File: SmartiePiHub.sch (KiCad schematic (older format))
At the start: 91 parts

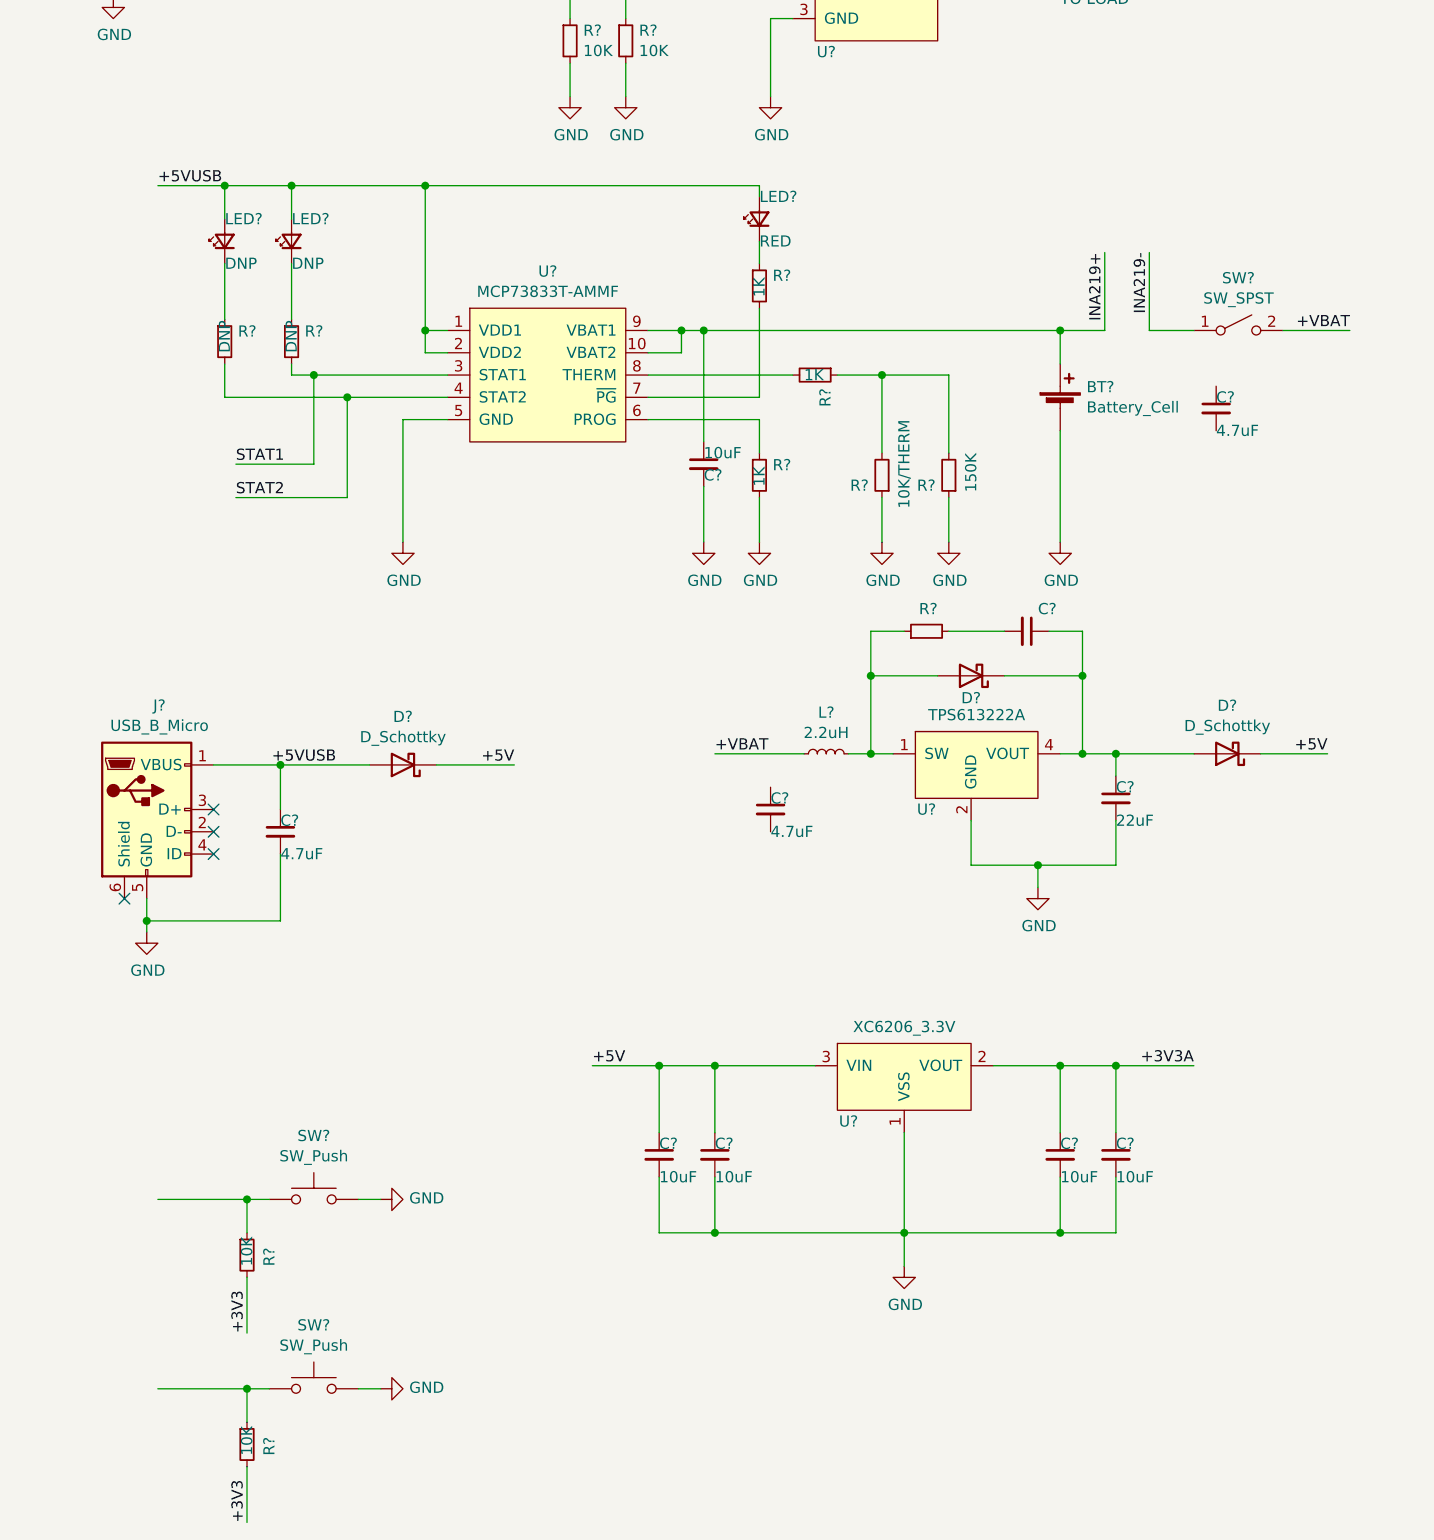
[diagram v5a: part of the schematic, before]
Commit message: cleaned up schematic a bit. Added some optional filter caps.
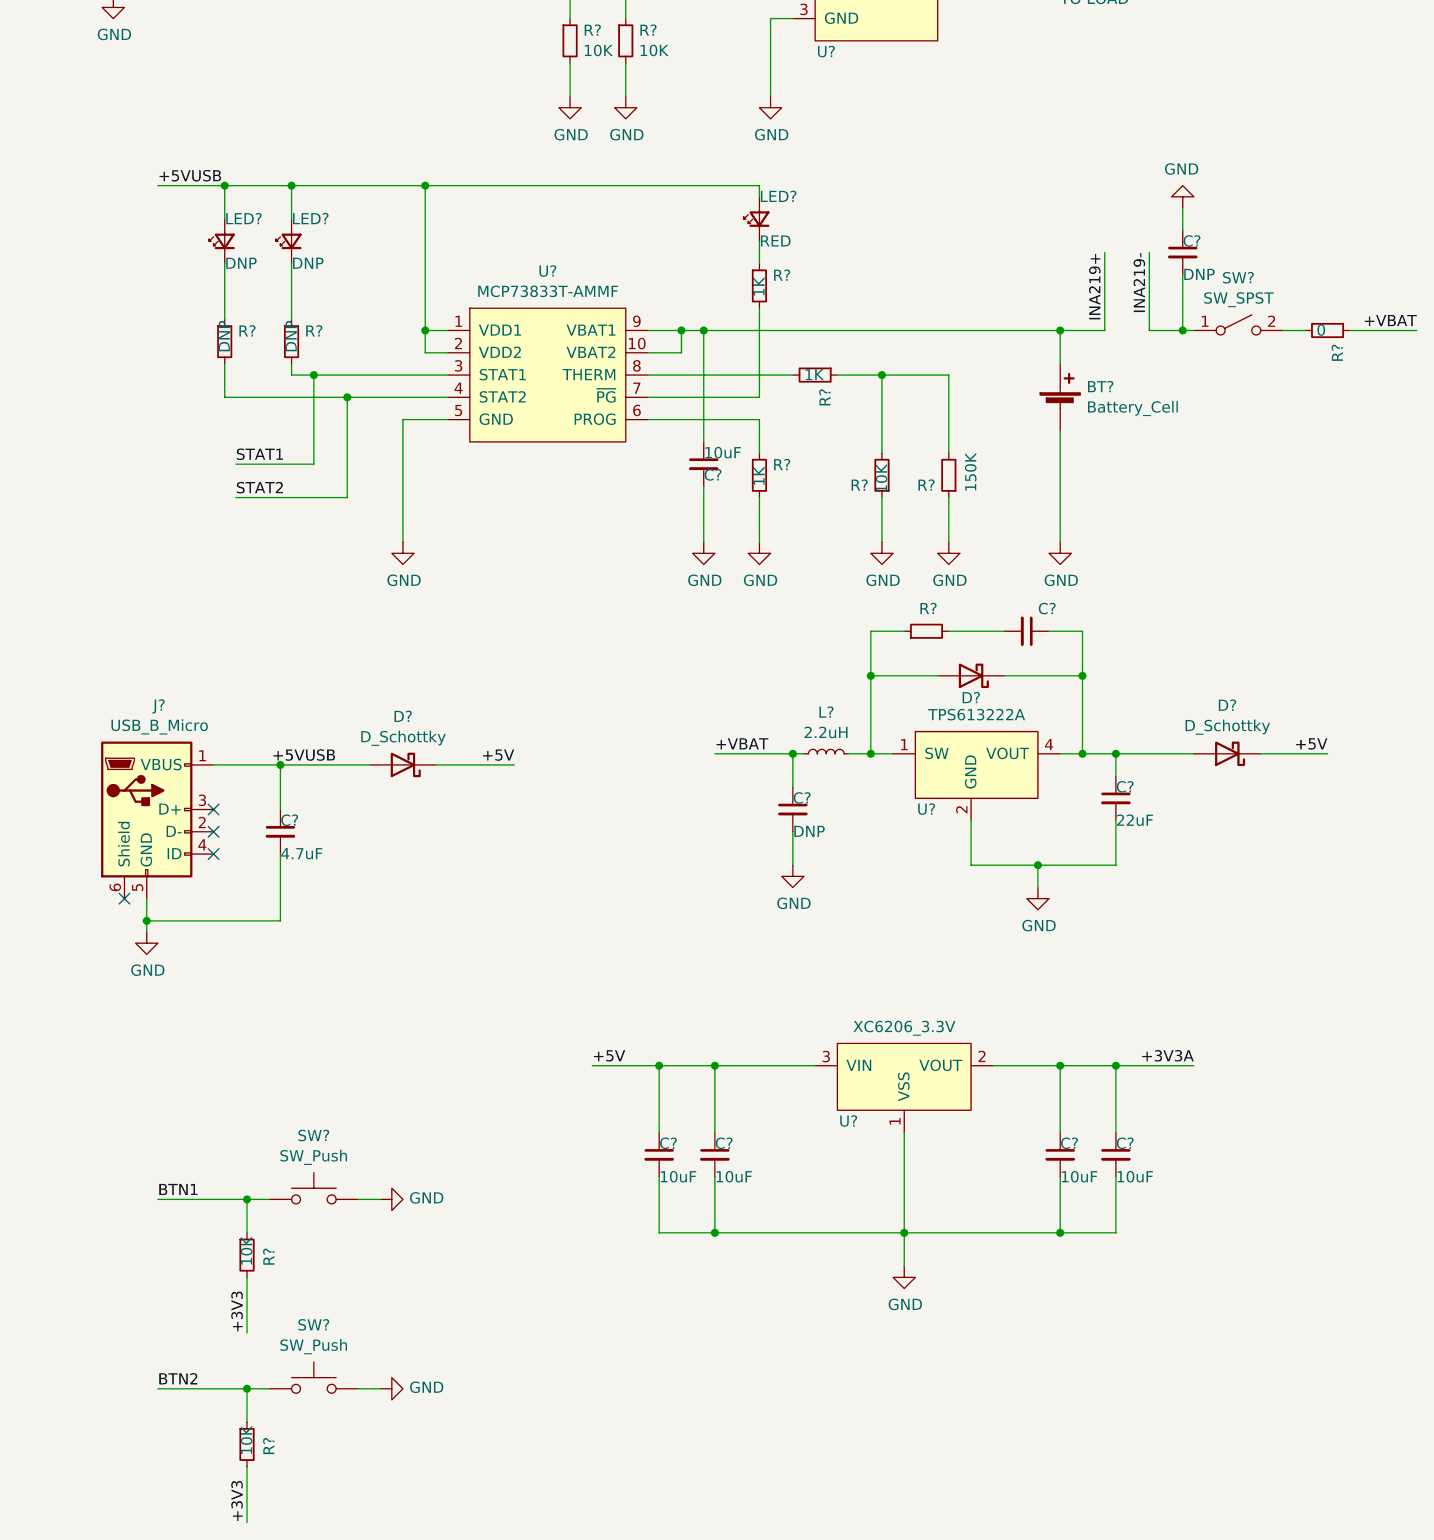
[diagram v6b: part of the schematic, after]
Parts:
- added R?: 0, symbol Device:R_Small
- C? (x2): value 4.7uF -> DNP
- R?: value 10K/THERM -> 10K
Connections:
- net +VBAT: now also C?.1, R?.1; no longer SW?.2 (B)
- net GND: now also C?.1, C?.2
- net INA219-: now also C?.2
- net BTN1: now reaches R?.1, SW?.1
- net BTN2: now reaches R?.1, SW?.1
- new net: R?.2, SW?.2 (B)
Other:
- moved on the sheet: C?
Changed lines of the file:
@@
 P 13850 5200
 F 0 "R?" H 13909 5246 50  0000 L CNN
-F 1 "10K/THERM" V 13750 4950 50  0000 L CNN
+F 1 "10K" V 13850 5150 50  0000 L CNN
 F 2 "" H 13850 5200 50  0001 C CNN
 F 3 "~" H 13850 5200 50  0001 C CNN
@@
 Wire Wire Line
 	13050 4550 14650 4550
-Text Label 15950 4550 2    50   ~ 0
+Text Label 16250 4550 2    50   ~ 0
 +VBAT
 $Comp
@@
 	13900 6450 13800 6450
 Wire Wire Line
-	13500 6450 13100 6450
+	13500 6450 13450 6450
 Text Label 13100 6450 0    50   ~ 0
 +VBAT
@@
 L Device:C_Small C?
 U 1 1 5FC8A77E
-P 13350 6700
-F 0 "C?" H 13350 6750 50  0000 L CNN
-F 1 "4.7uF" H 13350 6600 50  0000 L CNN
-F 2 "" H 13350 6700 50  0001 C CNN
-F 3 "~" H 13350 6700 50  0001 C CNN
-	1    13350 6700
+P 13450 6700
+F 0 "C?" H 13450 6750 50  0000 L CNN
+F 1 "DNP" H 13450 6600 50  0000 L CNN
+F 2 "" H 13450 6700 50  0001 C CNN
+F 3 "~" H 13450 6700 50  0001 C CNN
+	1    13450 6700
 	1    0    0    -1
 $EndComp
@@
 L Device:C_Small C?
 U 1 1 5FC8B279
-P 15350 4900
-F 0 "C?" H 15350 4950 50  0000 L CNN
-F 1 "4.7uF" H 15350 4800 50  0000 L CNN
-F 2 "" H 15350 4900 50  0001 C CNN
-F 3 "~" H 15350 4900 50  0001 C CNN
-	1    15350 4900
+P 15200 4200
+F 0 "C?" H 15200 4250 50  0000 L CNN
+F 1 "DNP" H 15200 4100 50  0000 L CNN
+F 2 "" H 15200 4200 50  0001 C CNN
+F 3 "~" H 15200 4200 50  0001 C CNN
+	1    15200 4200
 	1    0    0    -1
 $EndComp
@@
 +3V3
 Wire Wire Line
-	15250 4550 15050 4550
-Wire Wire Line
-	15650 4550 15950 4550
+	15250 4550 15200 4550
+Wire Wire Line
+	15950 4550 16250 4550
 $Comp
 L Switch:SW_Push SW?
@@
 Wire Wire Line
 	4350 2600 5400 2600
+$Comp
+L Device:R_Small R?
+U 1 1 600AB810
+P 15850 4550
+F 0 "R?" H 15909 4596 50  0000 L CNN
+F 1 "0" V 15850 4500 50  0000 L CNN
+F 2 "" H 15850 4550 50  0001 C CNN
+F 3 "~" H 15850 4550 50  0001 C CNN
+	1    15850 4550
+	0    1    1    0
+$EndComp
+Wire Wire Line
+	15750 4550 15650 4550
+Wire Wire Line
+	15200 4300 15200 4550
+Connection ~ 15200 4550
+Wire Wire Line
+	15200 4550 15050 4550
+Wire Wire Line
+	15200 4100 15200 4000
+$Comp
+L power:GND #PWR?
+U 1 1 6015BA49
+P 15200 4000
+F 0 "#PWR?" H 15200 3750 50  0001 C CNN
+F 1 "GND" H 15205 3827 50  0000 C CNN
+F 2 "" H 15200 4000 50  0001 C CNN
+F 3 "" H 15200 4000 50  0001 C CNN
+	1    15200 4000
+	-1   0    0    1
+$EndComp
+Wire Wire Line
+	13450 6600 13450 6450
+Connection ~ 13450 6450
+Wire Wire Line
+	13450 6450 13100 6450
+Wire Wire Line
+	13450 6800 13450 6950
+$Comp
+L power:GND #PWR?
+U 1 1 601B5163
+P 13450 6950
+F 0 "#PWR?" H 13450 6700 50  0001 C CNN
+F 1 "GND" H 13455 6777 50  0000 C CNN
+F 2 "" H 13450 6950 50  0001 C CNN
+F 3 "" H 13450 6950 50  0001 C CNN
+	1    13450 6950
+	1    0    0    -1
+$EndComp
+Text Label 10600 8450 0    50   ~ 0
+BTN1
+Text Label 10600 9300 0    50   ~ 0
+BTN2
 $EndSCHEMATC

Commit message: adding footprints
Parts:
- removed J?: USB_B_Micro, symbol Connector:USB_B_Micro
- added CN4: USB_C_Plug_USB2.0, SmartiePiHub:USB4125_TYPE_C, symbol Connector:USB_C_Plug_USB2.0
- added D?: WS2812B, LED_SMD:LED_WS2812B_PLCC4_5.0x5.0mm_P3.2mm, symbol LED:WS2812B
- C1, C10, C11, C12, C13, C14, C15, C16, C17, C18, C19, C2, C20, C21, C22, C23, C24, C25, C26, C27, C28, C29, C3, C30, C31, C32, C33, C34, C4, C5, C6, C7, C8, C9: renamed from C?; footprint (none) -> Capacitor_SMD:C_0805_2012Metric_Pad1.15x1.40mm_HandSolder
- D1, D2, D3: renamed from D?; footprint (none) -> SmartiePiHub:onsemi-NRVB120VLSFT1G
- L1, L2: renamed from L?; footprint (none) -> Inductor_SMD:L_0603_1608Metric_Pad1.05x0.95mm_HandSolder
- L3, L4: renamed from L?; footprint (none) -> Inductor_SMD:L_0805_2012Metric
- L5: renamed from L?; footprint (none) -> Inductor_SMD:L_1008_2520Metric_Pad1.43x2.20mm_HandSolder
- LED1, LED2, LED3: renamed from LED?; footprint (none) -> LED_SMD:LED_0805_2012Metric_Pad1.15x1.40mm_HandSolder
- MIC1, MIC2: renamed from MIC?; footprint (none) -> SmartiePiHub:SPH1642HT5H
- R1, R10, R11, R12, R13, R14, R15, R16, R17, R18, R19, R2, R20, R21, R22, R23, R24, R25, R3, R4, R5, R6, R7, R8, R9: renamed from R?; footprint (none) -> Resistor_SMD:R_0805_2012Metric_Pad1.15x1.40mm_HandSolder
- U1: renamed from U?; footprint (none) -> SmartiePiHub:WM8960CGEFL&slash_V
- U2: renamed from U?; footprint (none) -> Package_SO:MSOP-10_3x3mm_P0.5mm
- U3: renamed from U?; footprint (none) -> SmartiePiHub:INA219_SOIC_8
- U4: renamed from U?; footprint (none) -> Package_TO_SOT_SMD:SOT-23
- U5: renamed from U?; footprint (none) -> SmartiePiHub:TPS613222_SOT23_5
- gave numbers to parts that had none: 10
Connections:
- net +5VUSB: now also CN4.A4 (VBUS), CN4.A9 (VBUS), CN4.B4 (VBUS), CN4.B9 (VBUS)
- net GND: now also CN4.A1 (GND), CN4.A12 (GND), CN4.B1 (GND), CN4.B12 (GND)
- net NEOPIXEL_DIN: now also D?.4 (DIN)
- no-connect marks 15 -> 16
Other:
- moved on the sheet: C24, D1

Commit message: more work on footprints
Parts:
- added D5, D6, D7, D8: WS2812B, LED_SMD:LED_WS2812B_PLCC4_5.0x5.0mm_P3.2mm, symbol LED:WS2812B
- BT1: footprint (none) -> SmartiePiHub:KEYSTONE_1123_BATTERY_HOLDER
- LS1: footprint (none) -> Connector_JST:JST_PH_S2B-PH-K_1x02_P2.00mm_Horizontal
- R24: value .1 -> 0.1/1% (PT2512FK-070R1L); footprint Resistor_SMD:R_0805_2012Metric_Pad1.15x1.40mm_HandSolder -> SmartiePiHub:2512
- gave numbers to parts that had none: 1
- renumbered 111 to CN5
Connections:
- net +5V: now also D4.1 (VDD), D5.1 (VDD), D6.1 (VDD), D7.1 (VDD), D8.1 (VDD)
- net GND: now also D4.3 (VSS), D5.3 (VSS), D6.3 (VSS), D7.3 (VSS), D8.3 (VSS)
- net at D4.2 (DOUT): now also D5.4 (DIN)
- new net: D5.2 (DOUT), D6.4 (DIN)
- new net: D6.2 (DOUT), D7.4 (DIN)
- new net: D7.2 (DOUT), D8.4 (DIN)
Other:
- moved on the sheet: D4
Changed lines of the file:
@@
 F 0 "LS1" H 11470 2446 50  0000 L CNN
 F 1 "Speaker" H 11470 2355 50  0000 L CNN
-F 2 "" H 11300 2250 50  0001 C CNN
+F 2 "Connector_JST:JST_PH_S2B-PH-K_1x02_P2.00mm_Horizontal" H 11300 2250 50  0001 C CNN
 F 3 "~" H 11290 2400 50  0001 C CNN
 	1    11300 2450
@@
 P 14650 2800
 F 0 "R24" H 14720 2846 50  0000 L CNN
-F 1 ".1" V 14650 2750 50  0000 L CNN
-F 2 "Resistor_SMD:R_0805_2012Metric_Pad1.15x1.40mm_HandSolder" V 14580 2800 50  0001 C CNN
+F 1 "0.1/1% (PT2512FK-070R1L)" V 14650 2750 50  0000 L CNN
+F 2 "SmartiePiHub:2512" V 14580 2800 50  0001 C CNN
 F 3 "~" H 14650 2800 50  0001 C CNN
 	1    14650 2800
@@
 F 0 "BT1" H 14768 4996 50  0000 L CNN
 F 1 "Battery_Cell" H 14768 4905 50  0000 L CNN
-F 2 "" V 14650 4960 50  0001 C CNN
+F 2 "SmartiePiHub:KEYSTONE_1123_BATTERY_HOLDER" V 14650 4960 50  0001 C CNN
 F 3 "~" V 14650 4960 50  0001 C CNN
 	1    14650 4900
@@
 	2250 700  2250 1100
 $Comp
-L smartie-pi-raspi:RPI 111
+L smartie-pi-raspi:RPI CN5
 U 1 1 5F2DA592
 P 3350 2300
-F 0 "111" H 3400 3765 50  0000 C CNN
+F 0 "CN5" H 3400 3765 50  0000 C CNN
 F 1 "RPI" H 3400 3674 50  0000 C CNN
 F 2 "" H 3350 2300 50  0001 C CNN
@@
 NoConn ~ 9450 8150
 $Comp
-L LED:WS2812B D?
+L LED:WS2812B D4
 U 1 1 61B4542F
-P 5800 1000
-F 0 "D?" H 6144 1046 50  0000 L CNN
-F 1 "WS2812B" H 6144 955 50  0000 L CNN
-F 2 "LED_SMD:LED_WS2812B_PLCC4_5.0x5.0mm_P3.2mm" H 5850 700 50  0001 L TNN
-F 3 "https://cdn-shop.adafruit.com/datasheets/WS2812B.pdf" H 5900 625 50  0001 L TNN
-	1    5800 1000
-	1    0    0    -1
-$EndComp
-Text Label 4900 1000 0    50   ~ 0
+P 9200 1100
+F 0 "D4" H 9544 1146 50  0000 L CNN
+F 1 "WS2812B" H 9544 1055 50  0000 L CNN
+F 2 "LED_SMD:LED_WS2812B_PLCC4_5.0x5.0mm_P3.2mm" H 9250 800 50  0001 L TNN
+F 3 "https://cdn-shop.adafruit.com/datasheets/WS2812B.pdf" H 9300 725 50  0001 L TNN
+	1    9200 1100
+	1    0    0    -1
+$EndComp
+Text Label 8300 1100 0    50   ~ 0
 NEOPIXEL_DIN
 Wire Wire Line
-	4900 1000 5500 1000
+	8300 1100 8900 1100
+$Comp
+L LED:WS2812B D5
+U 1 1 61BA146D
+P 10100 1100
+F 0 "D5" H 10444 1146 50  0000 L CNN
+F 1 "WS2812B" H 10444 1055 50  0000 L CNN
+F 2 "LED_SMD:LED_WS2812B_PLCC4_5.0x5.0mm_P3.2mm" H 10150 800 50  0001 L TNN
+F 3 "https://cdn-shop.adafruit.com/datasheets/WS2812B.pdf" H 10200 725 50  0001 L TNN
+	1    10100 1100
+	1    0    0    -1
+$EndComp
+$Comp
+L LED:WS2812B D6
+U 1 1 61BA1C60
+P 11000 1100
+F 0 "D6" H 11344 1146 50  0000 L CNN
+F 1 "WS2812B" H 11344 1055 50  0000 L CNN
+F 2 "LED_SMD:LED_WS2812B_PLCC4_5.0x5.0mm_P3.2mm" H 11050 800 50  0001 L TNN
+F 3 "https://cdn-shop.adafruit.com/datasheets/WS2812B.pdf" H 11100 725 50  0001 L TNN
+	1    11000 1100
+	1    0    0    -1
+$EndComp
+$Comp
+L LED:WS2812B D7
+U 1 1 61BA261D
+P 11900 1100
+F 0 "D7" H 12244 1146 50  0000 L CNN
+F 1 "WS2812B" H 12244 1055 50  0000 L CNN
+F 2 "LED_SMD:LED_WS2812B_PLCC4_5.0x5.0mm_P3.2mm" H 11950 800 50  0001 L TNN
+F 3 "https://cdn-shop.adafruit.com/datasheets/WS2812B.pdf" H 12000 725 50  0001 L TNN
+	1    11900 1100
+	1    0    0    -1
+$EndComp
+$Comp
+L LED:WS2812B D8
+U 1 1 61BA3357
+P 12800 1100
+F 0 "D8" H 13144 1146 50  0000 L CNN
+F 1 "WS2812B" H 13144 1055 50  0000 L CNN
+F 2 "LED_SMD:LED_WS2812B_PLCC4_5.0x5.0mm_P3.2mm" H 12850 800 50  0001 L TNN
+F 3 "https://cdn-shop.adafruit.com/datasheets/WS2812B.pdf" H 12900 725 50  0001 L TNN
+	1    12800 1100
+	1    0    0    -1
+$EndComp
+Wire Wire Line
+	9500 1100 9800 1100
+Wire Wire Line
+	10400 1100 10700 1100
+Wire Wire Line
+	11300 1100 11600 1100
+Wire Wire Line
+	12200 1100 12500 1100
+Wire Wire Line
+	9200 800  10100 800
+Wire Wire Line
+	10100 800  11000 800
+Connection ~ 10100 800
+Wire Wire Line
+	11000 800  11900 800
+Connection ~ 11000 800
+Wire Wire Line
+	11900 800  12800 800
+Connection ~ 11900 800
+Wire Wire Line
+	9200 1400 10100 1400
+Wire Wire Line
+	10100 1400 10550 1400
+Connection ~ 10100 1400
+Wire Wire Line
+	11000 1400 11900 1400
+Connection ~ 11000 1400
+Wire Wire Line
+	11900 1400 12800 1400
+Connection ~ 11900 1400
+Text Label 9600 800  2    50   ~ 0
++5V
+$Comp
+L power:GND #PWR0136
+U 1 1 61DCEDF2
+P 10550 1400
+F 0 "#PWR0136" H 10550 1150 50  0001 C CNN
+F 1 "GND" V 10555 1272 50  0000 R CNN
+F 2 "" H 10550 1400 50  0001 C CNN
+F 3 "" H 10550 1400 50  0001 C CNN
+	1    10550 1400
+	1    0    0    -1
+$EndComp
+Connection ~ 10550 1400
+Wire Wire Line
+	10550 1400 11000 1400
 $EndSCHEMATC
